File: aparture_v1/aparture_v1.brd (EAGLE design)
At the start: 160 x 100 mm, 89 parts, among them IC1 LD117AS33TR, IC3 LTC1966CMS8, T1 BT138-V, T2 BT138-V, T3 BT138-V, T4 BT138-V, T5 BT138-V, T6 BT138-V, T7 BT138-V, T8 BT138-V

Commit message: brd and sch made for 80*70mm boards, separated controller and triacs
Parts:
- removed C5: C0.22uF, resistor:C0805
- removed C6: C33pF, resistor:C0805
- removed C7: C100uF, resistor:153CLV-0605
- removed C8, C9: C0.1uF, resistor:C0805
- removed CUR_SENS_JACK: (no value), SparkFun-Connectors:AUDIO-JACK-3.5MM-SMD
- removed D1: (no value), microbuilder:SOT363
- removed IC1: LD117AS33TR, v-reg:SOT223
- removed IC3: LTC1966CMS8, linear-technology-2:MSOP8
- removed J1: (no value), SparkFun-Connectors:SIMHOLDER
- removed LED1, LED2, LED3, LED4, LED5, LED6, LED7, LED8: (no value), adafruit:LED3MM
- removed LOAD1, LOAD2, LOAD3, LOAD4, LOAD5, LOAD6, LOAD7, LOAD8: (no value), con-ptr500:AK300/2
- removed R1, R12, R15, R18, R21, R24, R6, R9: R120, resistor:M0805
- removed R28: R1K, resistor:M0805
- removed R4: R100K, resistor:M0805
- removed SIM900TEC: 1296-T60, con-leotronics:1296-60
- removed U$1: ARDUINO_PRO_MINI, tigorcustom:ARDUINO_PRO_MINI
- removed VOL_REG_SIM900: DCDCMODULE, bontor:DCDCMODULE
- added IN, OUT: (no value), con-ptr500:AK300/10
- added JP3: SMPS_OUT, pinhead:1X02
- added OK10, OK9: MOC3021M, optocoupler:DIL06
- added T10: BT138-V, triac:TO220BV
- C1, C2: value C10uF -> C0.1uF
- JP2: value SMPS_OUT -> (none); device pinhead:1X02 -> pinhead:2X05
- R27: value R50 -> R2.4K
- R29: value R2K -> R180
- R30: value R120 -> R2.4K
- R5: value R100K -> R180
- T9: value (none) -> BT138-V; device transistor-neu-to92:SOT23-BEC -> triac:TO220BV
- moved R30 488.8 mm to (25.7, 63.4)
- moved T9 487.3 mm to (54.5, 56.1), turned to 180 degrees
- moved R29 479.7 mm to (24.6, 66.8)
- moved R5 408.8 mm to (35.6, 67.6)
- moved R27 402.1 mm to (41.5, 67.5)
- moved R22 369.1 mm to (57.4, 45.3), turned to 90 degrees
- moved R23 367.3 mm to (57.4, 50.2), turned to 90 degrees
- moved R26 349.0 mm to (24.2, 50.9), turned to 90 degrees
- moved R25 349.0 mm to (23.9, 46.3), turned to 90 degrees
- moved C15 348.0 mm to (61.0, 46.2), turned to 90 degrees
- moved T8 346.0 mm to (30.9, 49.2), turned to 90 degrees
- moved C13 345.6 mm to (60.8, 34.4), turned to 90 degrees
- moved R20 344.1 mm to (23.5, 38.3), turned to 90 degrees
- moved R16 341.1 mm to (57.2, 32.4), turned to 90 degrees
- moved R17 331.8 mm to (57.3, 38.0), turned to 90 degrees
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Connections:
- removed net 3V3: C2.1, IC1.4, IC3.7, LED1.A, LED2.A, LED3.A, LED4.A, LED5.A, LED6.A, LED7.A, LED8.A, R4.2, U$1.21
- removed net CTRL_PWRKEY: R30.1, U$1.19
- removed net CUR_SENS: CUR_SENS_JACK.RING, IC3.2, R27.2
- removed net CUR_SENS_DC: C9.1, IC3.5, U$1.20
- removed net N$1: LED1.K, R1.1
- removed net N$10: LED2.K, R6.1
- removed net N$11: OK2.1, R6.2
- removed net N$16: LED3.K, R9.1
- removed net N$17: OK3.1, R9.2
- removed net N$2: OK1.1, R1.2
- removed net N$22: LED4.K, R12.1
- removed net N$23: OK4.1, R12.2
- removed net N$28: LED5.K, R15.1
- removed net N$29: OK5.1, R15.2
- removed net N$34: LED6.K, R18.1
- removed net N$35: OK6.1, R18.2
- removed net N$40: LED7.K, R21.1
- removed net N$41: OK7.1, R21.2
- removed net N$46: LED8.K, R24.1
- removed net N$47: OK8.1, R24.2
- removed net N$7: C8.1, IC3.3, R27.1, R4.1, R5.2
- removed net N$8: R30.2, T9.B
- removed net PWRKEY: SIM900TEC.17, T9.C
- removed net SIM_CLK: D1.5, J1.C3, SIM900TEC.31
- removed net SIM_DATA: D1.4, J1.C7, SIM900TEC.29
- removed net SIM_RST: D1.3, J1.C2, SIM900TEC.27
- removed net SIM_RXD: SIM900TEC.41, U$1.1
- removed net SIM_TXD: R28.2, SIM900TEC.43
- removed net SIM_TXD_L: R28.1, R29.2, U$1.2
- removed net SIM_VDD: C5.1, C6.1, D1.1, J1.C1, SIM900TEC.25
- removed net VBAT: C7.+, SIM900TEC.1, SIM900TEC.3, SIM900TEC.5, SIM900TEC.7, SIM900TEC.9, VOL_REG_SIM900.VOUT
- new net CTRL_SW10: JP2.10, OK10.2
- new net CTRL_SW9: JP2.9, OK9.2
- new net N$52: IN.2, R8.2, T2.T2
- new net N$53: IN.3, R11.2, T3.T2
- new net N$54: IN.4, R14.2, T4.T2
- new net N$55: IN.8, R26.2, T8.T2
- new net N$56: IN.7, R23.2, T7.T2
- new net N$57: IN.6, R20.2, T6.T2
- new net N$58: IN.5, R17.2, T5.T2
- new net N$59: OK9.6, R5.1
- new net N$60: C1.1, R27.1, R5.2
- new net N$61: OK9.4, T9.G
- new net N$62: C1.2, OUT.9, T9.T1
- new net N$65: OK10.6, R29.1
- new net N$66: C2.1, R29.2, R30.1
- new net N$67: OK10.4, T10.G
- new net N$68: C2.2, OUT.10, T10.T1
- new net N$69: IN.9, R27.2, T9.T2
- new net N$70: IN.10, R30.2, T10.T2
- new net N$9: IN.1, R3.2, T1.T2
- net AC_IN: no longer R11.2, R14.2, R17.2, R20.2, R23.2, R26.2, R3.2, R8.2, T1.T2, T2.T2, T3.T2, T4.T2, T5.T2, T6.T2, T7.T2, T8.T2
- net CTRL_SW1: now also JP2.1; no longer U$1.5
- net CTRL_SW2: now also JP2.2; no longer U$1.6
- net CTRL_SW3: now also JP2.3; no longer U$1.7
- net CTRL_SW4: now also JP2.4; no longer U$1.8
- net CTRL_SW5: now also JP2.5; no longer U$1.9
- net CTRL_SW6: now also JP2.6; no longer U$1.10
- net CTRL_SW7: now also JP2.7; no longer U$1.11
- net CTRL_SW8: now also JP2.8; no longer U$1.12
- net GND: now also JP3.1; no longer C1.2, C2.2, C5.2, C6.2, C7.-, C8.2, C9.2, CUR_SENS_JACK.SLEEVE, D1.2, IC1.1, IC3.1, IC3.4, IC3.6, IC3.8, J1.C5, JP2.1, R29.1, R5.1, SIM900TEC.10, SIM900TEC.2, SIM900TEC.4, SIM900TEC.51, SIM900TEC.52, SIM900TEC.6, SIM900TEC.8, T9.E, U$1.23, U$1.4, VOL_REG_SIM900.GND#0, VOL_REG_SIM900.GND#1
- net N$15: now also OUT.2; no longer LOAD2.1
- net N$21: now also OUT.3; no longer LOAD3.1
- net N$27: now also OUT.4; no longer LOAD4.1
- net N$33: now also OUT.5; no longer LOAD5.1
- net N$39: now also OUT.6; no longer LOAD6.1
- net N$45: now also OUT.7; no longer LOAD7.1
- net N$51: now also OUT.8; no longer LOAD8.1
- net N$6: now also OUT.1; no longer LOAD1.1
- net NEUTRAL: no longer LOAD1.2, LOAD2.2, LOAD3.2, LOAD4.2, LOAD5.2, LOAD6.2, LOAD7.2, LOAD8.2
- net VDC: now also JP3.2, OK1.1, OK10.1, OK2.1, OK3.1, OK4.1, OK5.1, OK6.1, OK7.1, OK8.1, OK9.1; no longer C1.1, IC1.3, JP2.2, VOL_REG_SIM900.VIN
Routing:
- net VDC: track 0.00 -> 220.3 mm, vias 0 -> 2
- net N$62: track 0.00 -> 86.5 mm, vias 0 -> 1
- net N$33: track 0.00 -> 86.0 mm, vias 0 -> 3
- net N$6: track 0.00 -> 79.6 mm
- net N$21: track 0.00 -> 75.8 mm, vias 0 -> 1
- net N$45: track 0.00 -> 71.6 mm
- net N$57: track 0.00 -> 65.5 mm
- net N$52: track 0.00 -> 65.2 mm
- net N$70: track 0.00 -> 61.6 mm
- net N$55: track 0.00 -> 61.1 mm
- net N$54: track 0.00 -> 58.7 mm
- net CTRL_SW2: track 0.00 -> 54.4 mm
- net N$69: track 0.00 -> 46.3 mm
- net N$15: track 0.00 -> 44.8 mm
- net N$68: track 0.00 -> 43.2 mm
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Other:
- board size 160 x 100 mm -> 79.8 x 70.6 mm

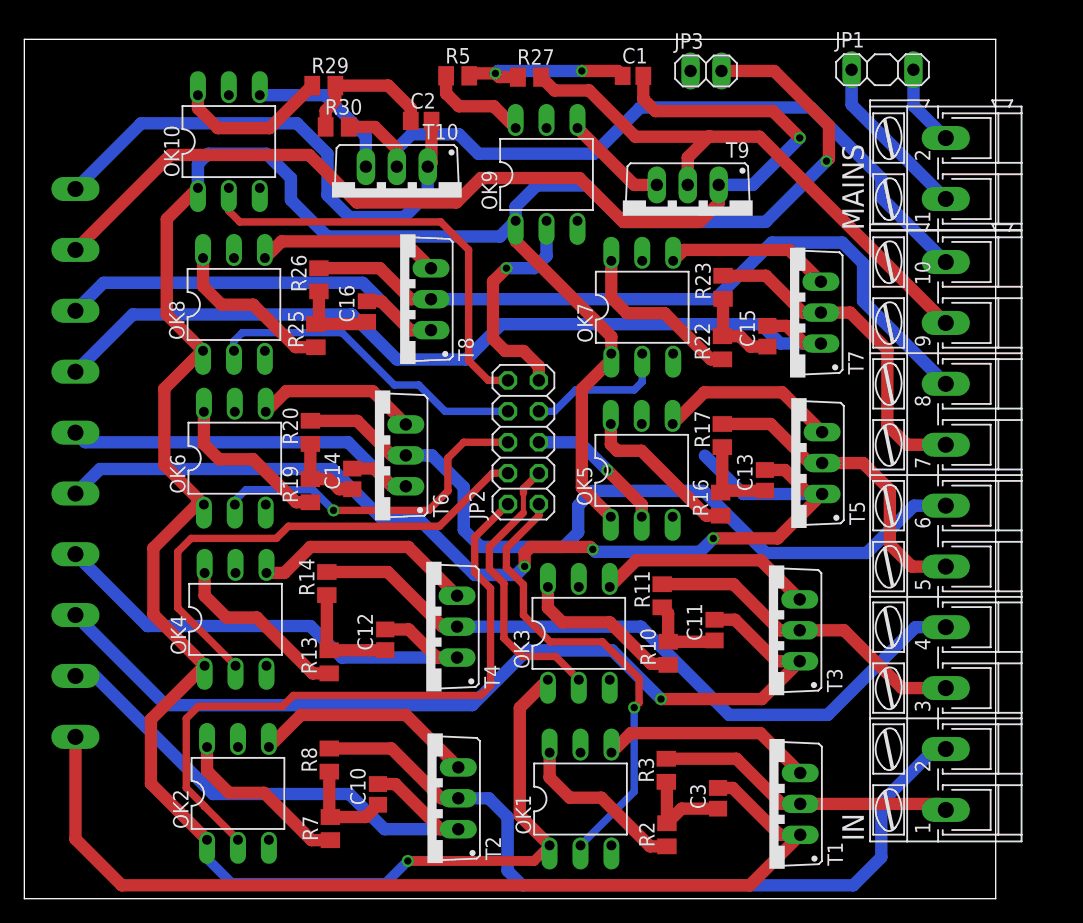
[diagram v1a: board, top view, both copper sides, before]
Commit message: resize boards
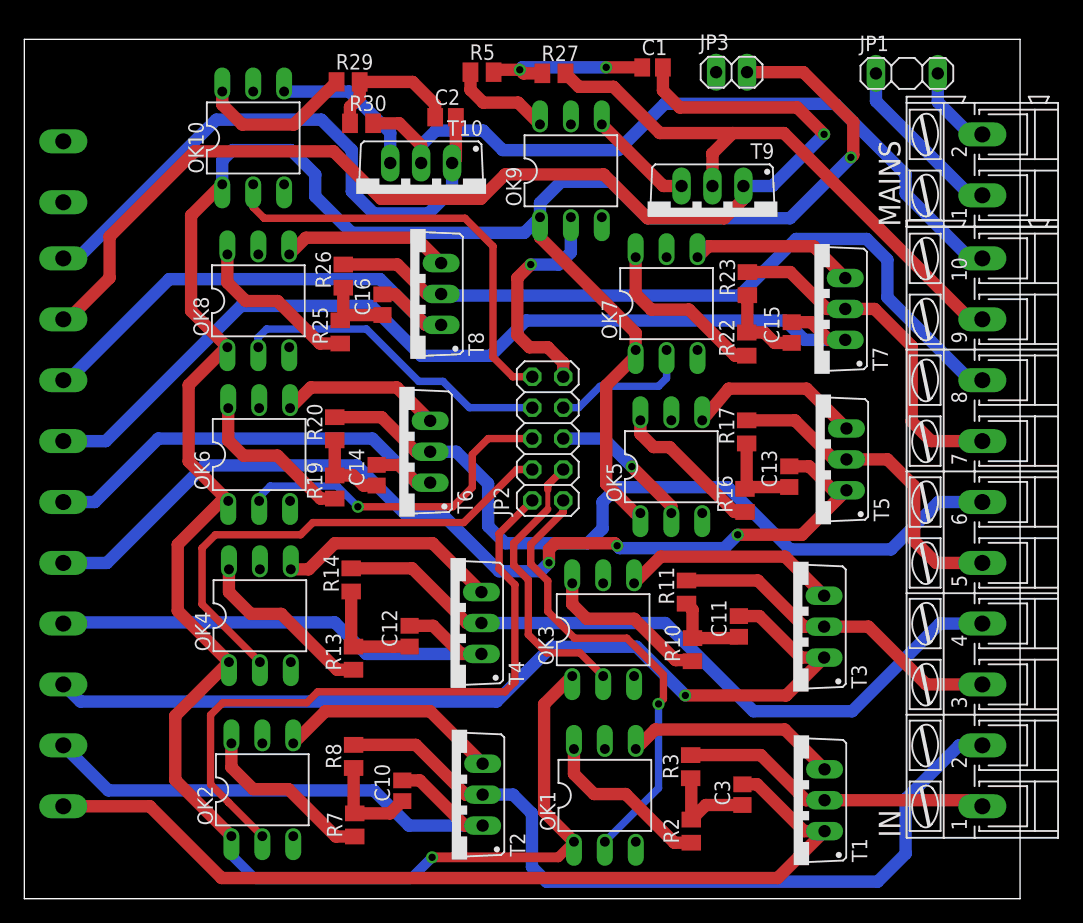
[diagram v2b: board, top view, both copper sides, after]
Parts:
- added DUMMY: (no value), con-ptr500:AK300/2
- moved OUT 5.79 mm to (3.20, 30.1)
- moved IN 3.01 mm to (78.7, 30.1)
- moved MAINS 3.01 mm to (78.7, 60.3)
- moved OK5 2.45 mm to (53.1, 35.5)
- moved JP3 2.10 mm to (58.1, 67.9)
- moved T9 2.03 mm to (56.5, 56.0)
- moved T7 2.02 mm to (64.9, 48.5)
- moved R5 2.02 mm to (37.6, 67.9)
- moved C13 2.02 mm to (62.8, 34.7)
- moved C2 2.02 mm to (34.6, 64.2)
- moved OK6 2.02 mm to (19.3, 36.5)
- moved R17 2.02 mm to (59.3, 38.4)
- moved R22 2.02 mm to (59.4, 45.6)
- moved R23 2.02 mm to (59.4, 50.5)
- moved R25 2.02 mm to (25.9, 46.6)
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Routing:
- net N$62: track 86.5 -> 94.2 mm
- net N$45: track 71.6 -> 77.4 mm
- net N$68: track 43.2 -> 48.7 mm
- net N$33: track 86.0 -> 80.5 mm
- net N$39: track 34.0 -> 38.8 mm
- net N$6: track 79.6 -> 74.9 mm
- net N$51: track 38.0 -> 41.9 mm
- net N$69: track 46.3 -> 47.7 mm
- net N$50: track 15.1 -> 13.9 mm
- net N$70: track 61.6 -> 62.6 mm
- net N$55: track 61.1 -> 62.1 mm
- net N$9: track 24.7 -> 25.7 mm
- net N$57: track 65.5 -> 66.5 mm
- net N$54: track 58.7 -> 59.7 mm
- net N$53: track 26.8 -> 27.8 mm
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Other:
- board size 79.8 x 70.6 mm -> 81.8 x 70.6 mm

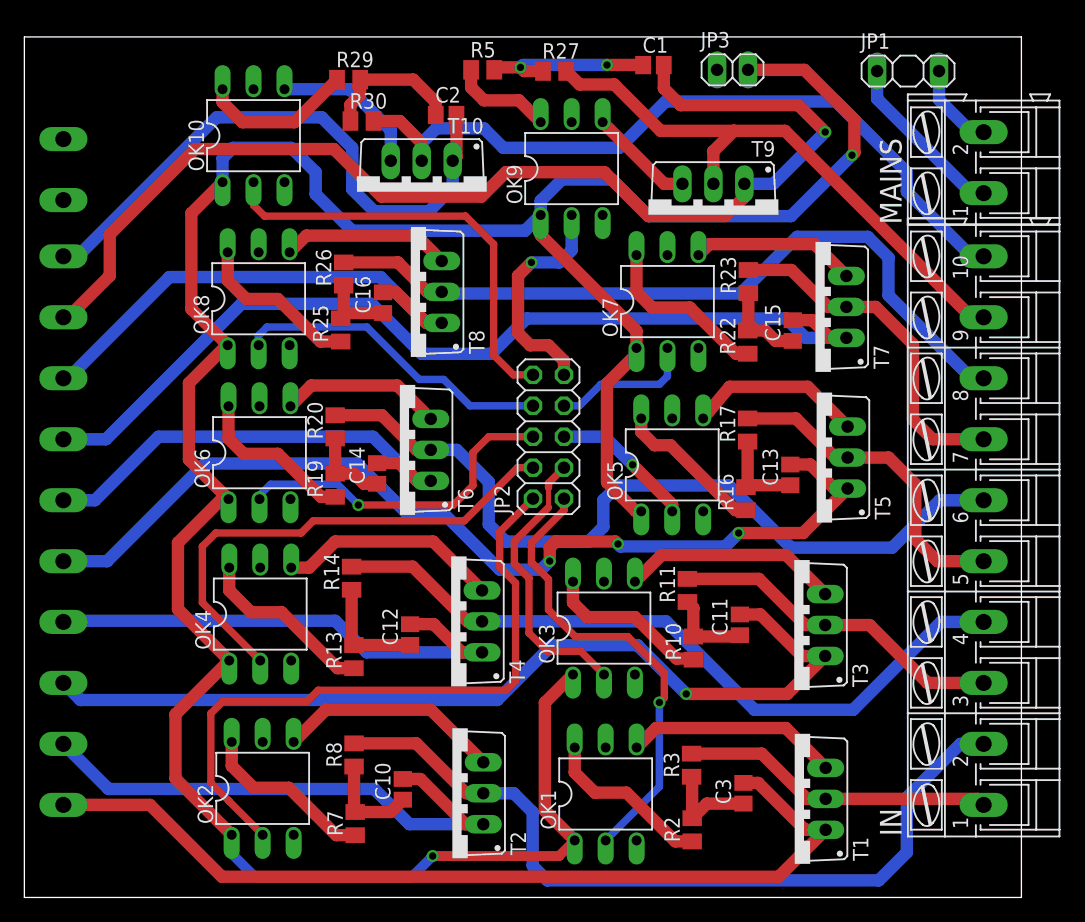
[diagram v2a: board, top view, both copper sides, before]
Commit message: resize to 68 mm
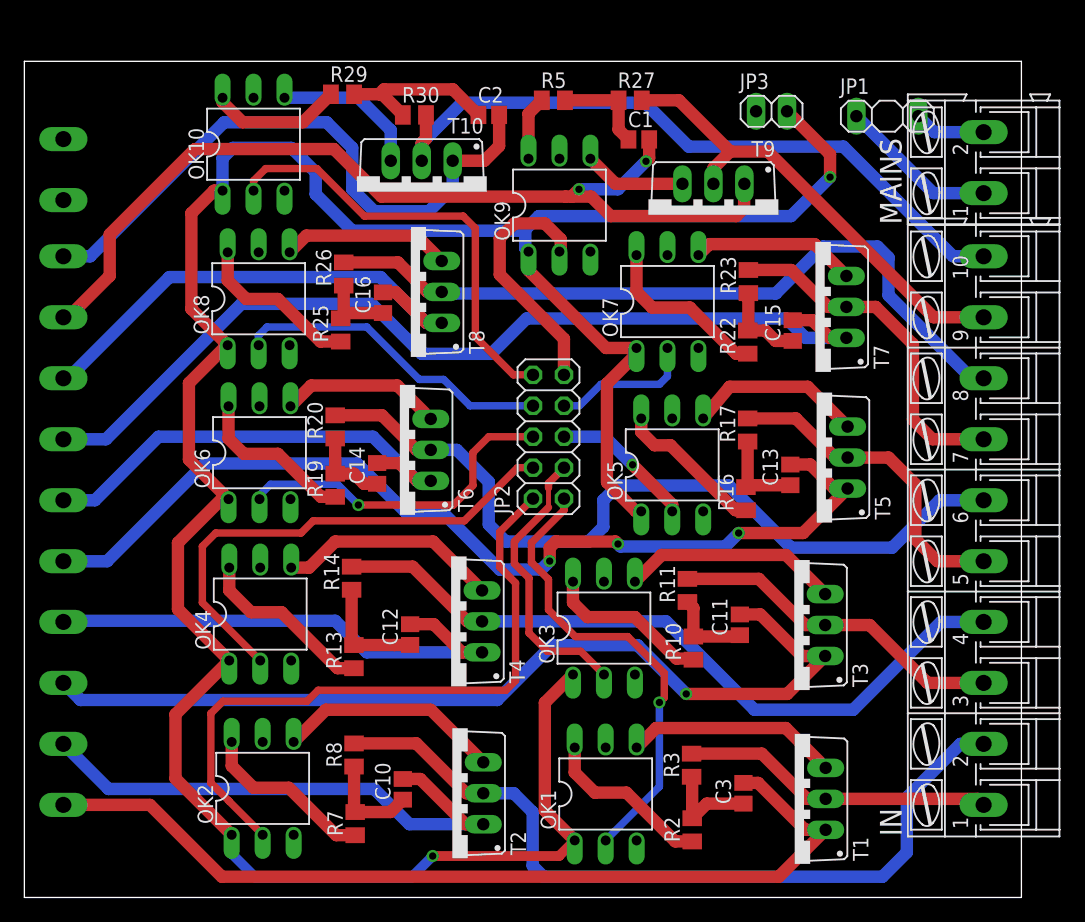
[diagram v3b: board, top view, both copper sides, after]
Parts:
- moved R27 6.65 mm to (49.7, 65.4)
- moved R5 6.32 mm to (43.4, 65.4)
- moved C1 6.22 mm to (50.4, 62.2)
- moved JP3 4.67 mm to (61.3, 64.5)
- moved R30 4.33 mm to (32.0, 64.2)
- moved JP1 4.07 mm to (70.8, 64.1)
- moved C2 3.50 mm to (38.1, 64.2)
- moved OK9 3.16 mm to (43.9, 56.8)
- moved R29 1.30 mm to (26.1, 65.9)
- moved OK10 0.70 mm to (18.8, 61.8)
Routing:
- net N$62: track 94.2 -> 77.8 mm, vias 1 -> 2
- net VDC: track 220.4 -> 209.4 mm
- net N$69: track 47.7 -> 38.6 mm
- net N$60: track 14.4 -> 7.95 mm, vias 2 -> 0
- net N$70: track 62.6 -> 59.0 mm
- net N$59: track 8.34 -> 5.24 mm
- net N$68: track 48.7 -> 51.8 mm
- net N$66: track 11.7 -> 13.9 mm
- net CTRL_SW9: track 18.7 -> 20.5 mm, vias 1 -> 0
- net N$65: track 12.6 -> 10.9 mm
- net N$55: track 62.1 -> 61.4 mm
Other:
- board size 81.8 x 70.6 mm -> 81.8 x 68.6 mm
